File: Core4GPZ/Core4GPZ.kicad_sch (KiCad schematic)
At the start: 3 parts, among them U1 core4, U2 MPX4250

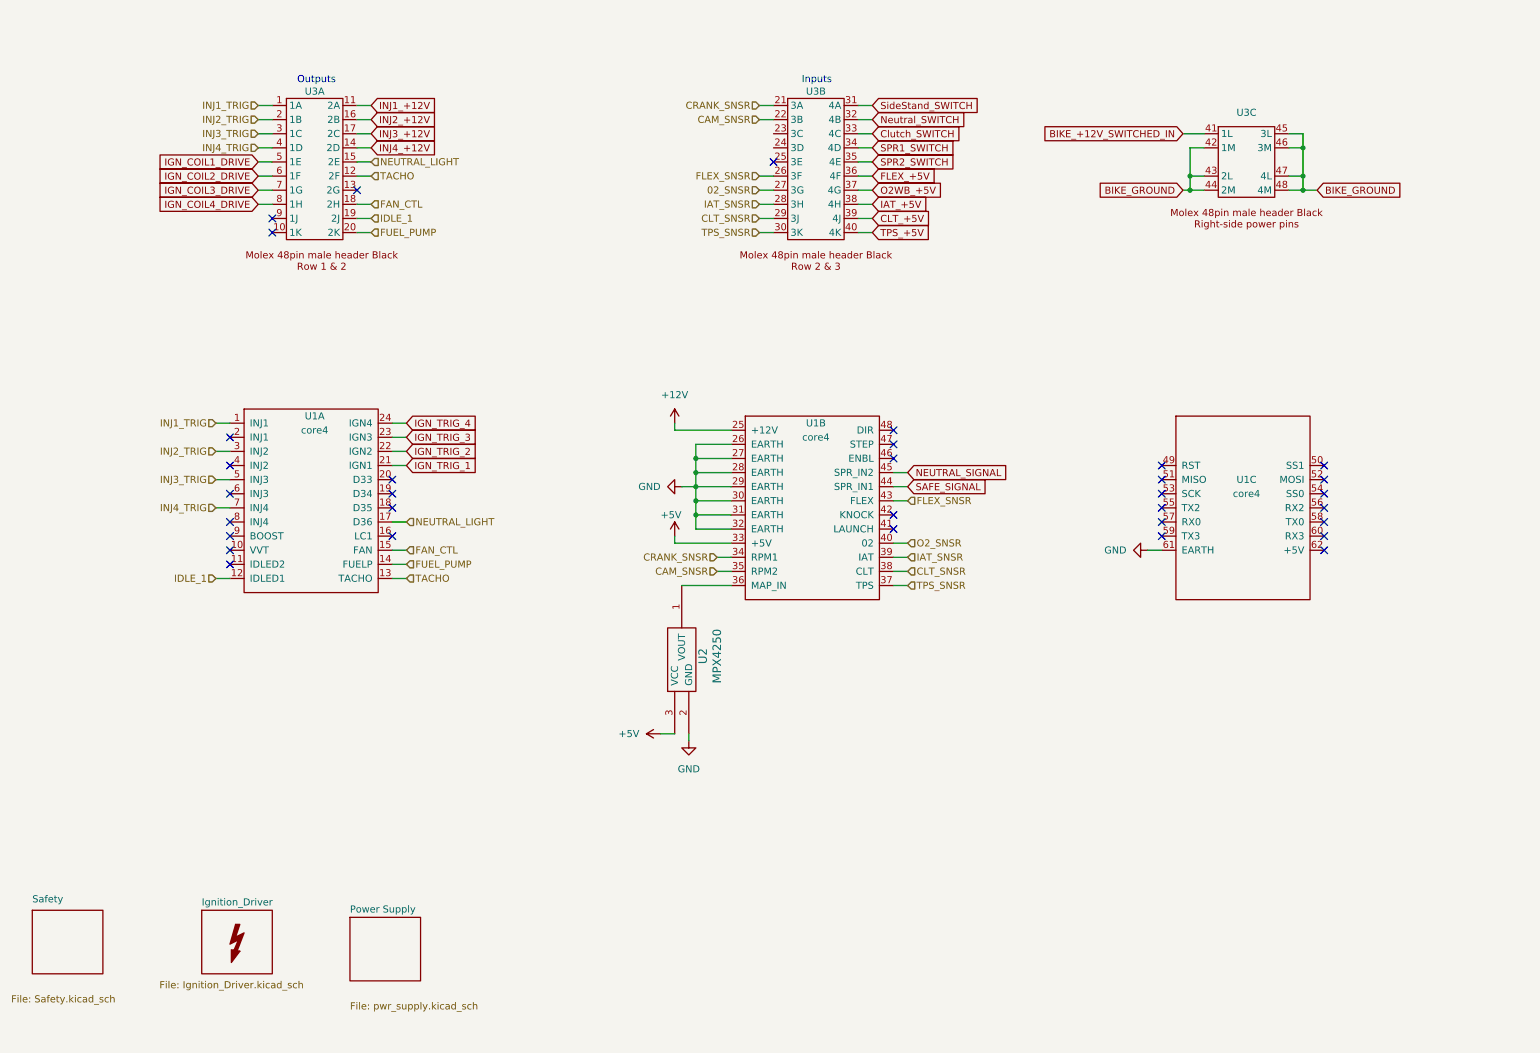
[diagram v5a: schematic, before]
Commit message: Added VR Conditionner for Cam/Crank SNSR
Added some jumper for prototyping and testing purposes
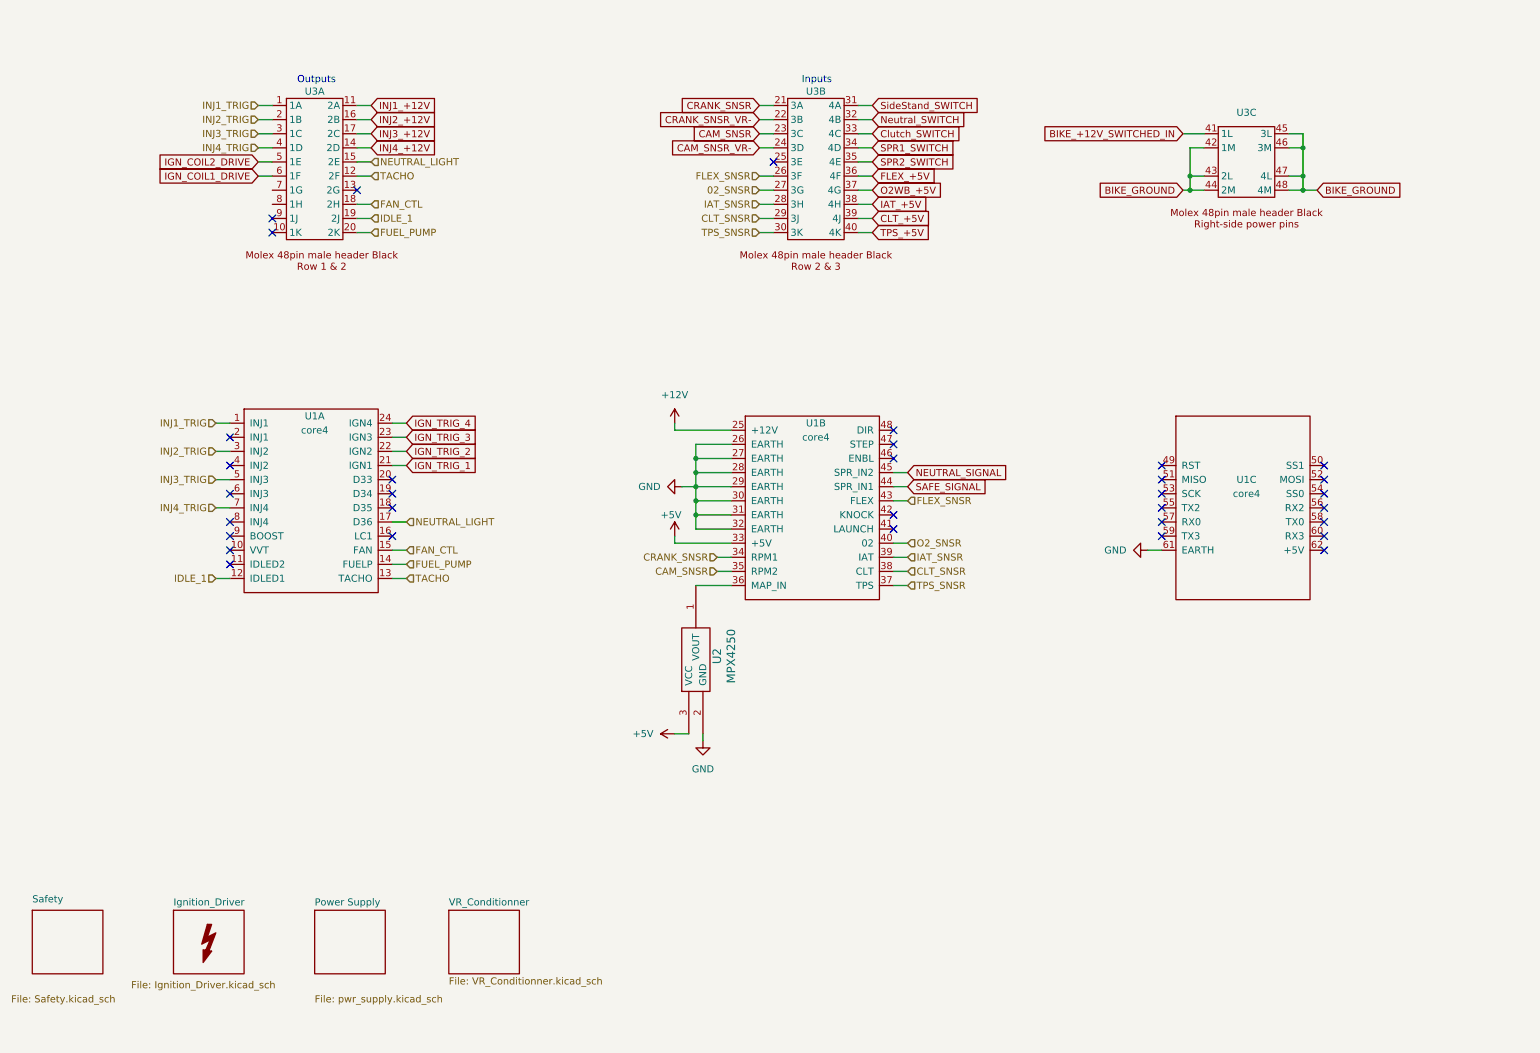
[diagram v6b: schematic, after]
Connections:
- net CAM_SNSR: now also U3.23 (3C); no longer U3.22 (3B)
- net IGN_COIL1_DRIVE: now also U3.6 (1F); no longer U3.5 (1E)
- net IGN_COIL2_DRIVE: now also U3.5 (1E); no longer U3.6 (1F)
- net CAM_SNSR_VR-: now reaches U3.24 (3D)
- net IGN_COIL3_DRIVE: no longer names the net of U3.7 (1G)
- net IGN_COIL4_DRIVE: no longer names the net of U3.8 (1H)
- new net CRANK_SNSR_VR-: U3.22 (3B)
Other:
- added sheet VR_Conditionner (VR_Conditionner.kicad_sch)
- moved on the sheet: U2

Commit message: Started Implementation of VR Conditionner
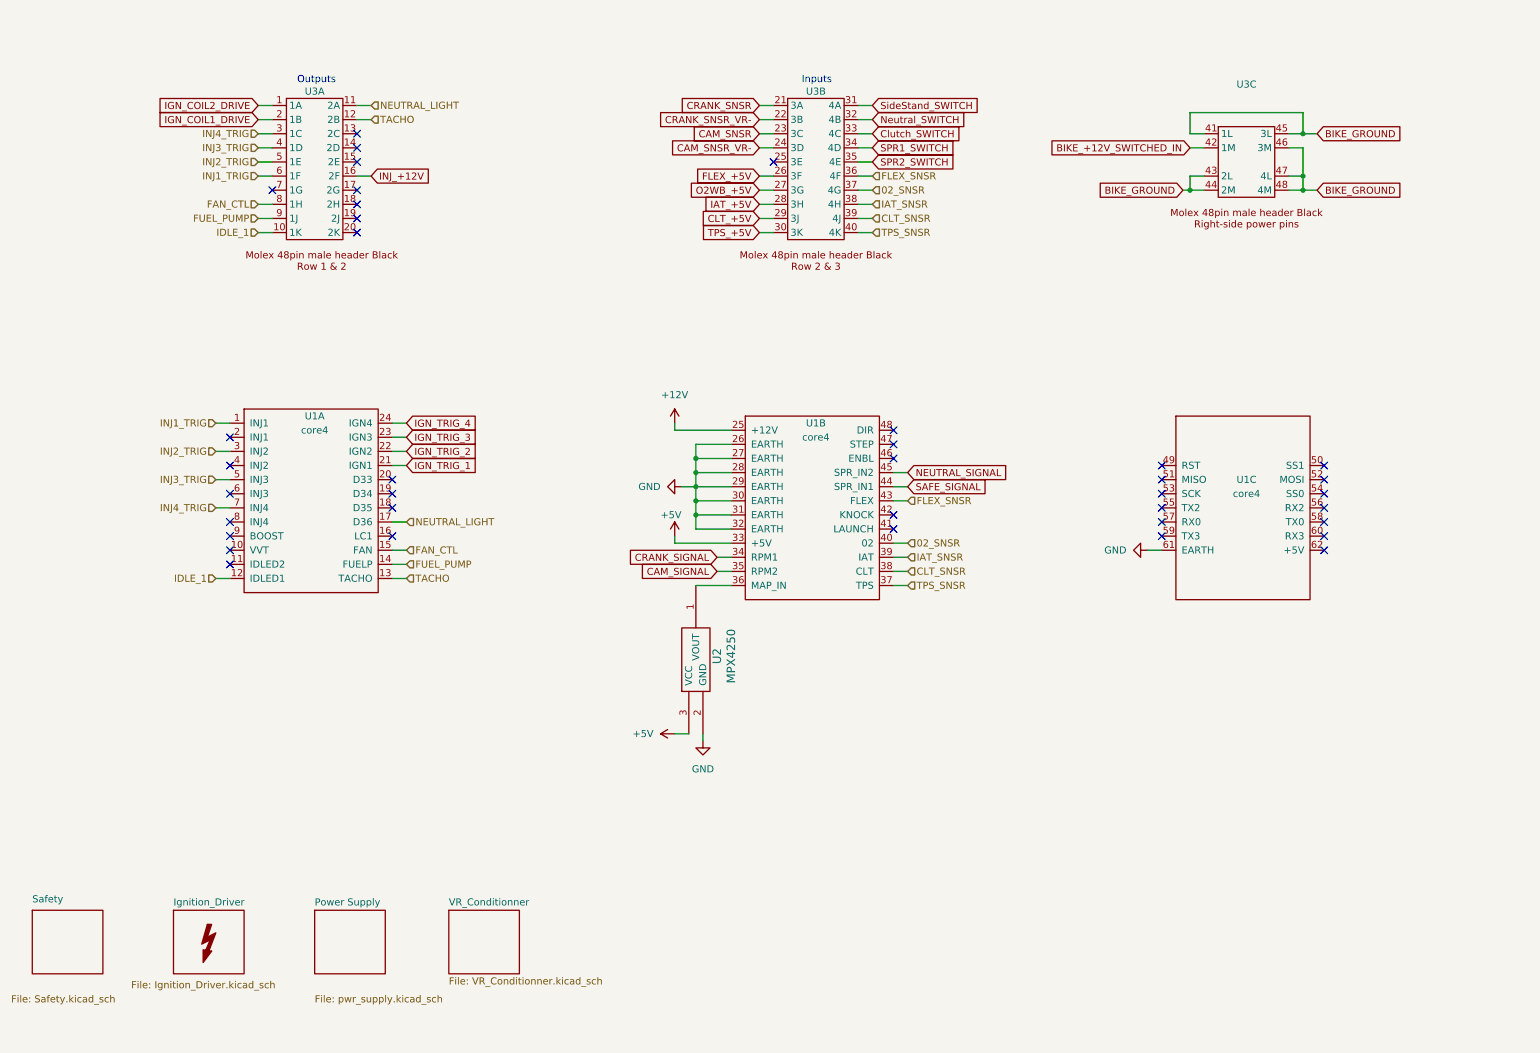
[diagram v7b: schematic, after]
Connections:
- net INJ1_+12V is gone; now on net NEUTRAL_LIGHT: U3.11 (2A)
- net O2_SNSR is gone; now on net 02_SNSR: U1.40 (02)
- net 02_SNSR: now also U3.37 (4G); no longer U3.27 (3G)
- net BIKE_+12V_SWITCHED_IN: now also U3.42 (1M); no longer U3.41 (1L)
- net BIKE_GROUND: now also U3.41 (1L); no longer U3.42 (1M)
- net CAM_SNSR: no longer U1.35 (RPM2)
- net CLT_+5V: now also U3.29 (3J); no longer U3.39 (4J)
- net CLT_SNSR: now also U3.39 (4J); no longer U3.29 (3J)
- net CRANK_SNSR: no longer U1.34 (RPM1)
- net FAN_CTL: now also U3.8 (1H); no longer U3.18 (2H)
- net FLEX_+5V: now also U3.26 (3F); no longer U3.36 (4F)
- net FLEX_SNSR: now also U3.36 (4F); no longer U3.26 (3F)
- net FUEL_PUMP: now also U3.9 (1J); no longer U3.20 (2K)
- net IAT_+5V: now also U3.28 (3H); no longer U3.38 (4H)
- net IAT_SNSR: now also U3.38 (4H); no longer U3.28 (3H)
- net IDLE_1: now also U3.10 (1K); no longer U3.19 (2J)
- net IGN_COIL1_DRIVE: now also U3.2 (1B); no longer U3.6 (1F)
- net IGN_COIL2_DRIVE: now also U3.1 (1A); no longer U3.5 (1E)
- net INJ1_TRIG: now also U3.6 (1F); no longer U3.1 (1A)
- net INJ2_TRIG: now also U3.5 (1E); no longer U3.2 (1B)
- net INJ3_TRIG: now also U3.4 (1D); no longer U3.3 (1C)
- net INJ4_TRIG: now also U3.3 (1C); no longer U3.4 (1D)
- net NEUTRAL_LIGHT: no longer U3.15 (2E)
- net O2WB_+5V: now also U3.27 (3G); no longer U3.37 (4G)
- net TPS_+5V: now also U3.30 (3K); no longer U3.40 (4K)
- net TPS_SNSR: now also U3.40 (4K); no longer U3.30 (3K)
- net INJ2_+12V renamed INJ_+12V
- net INJ3_+12V: no longer names the net of U3.17 (2G)
- net INJ4_+12V: no longer names the net of U3.14 (2D)
- new net CAM_SIGNAL: U1.35 (RPM2)
- new net CRANK_SIGNAL: U1.34 (RPM1)
- no-connect marks 33 -> 38

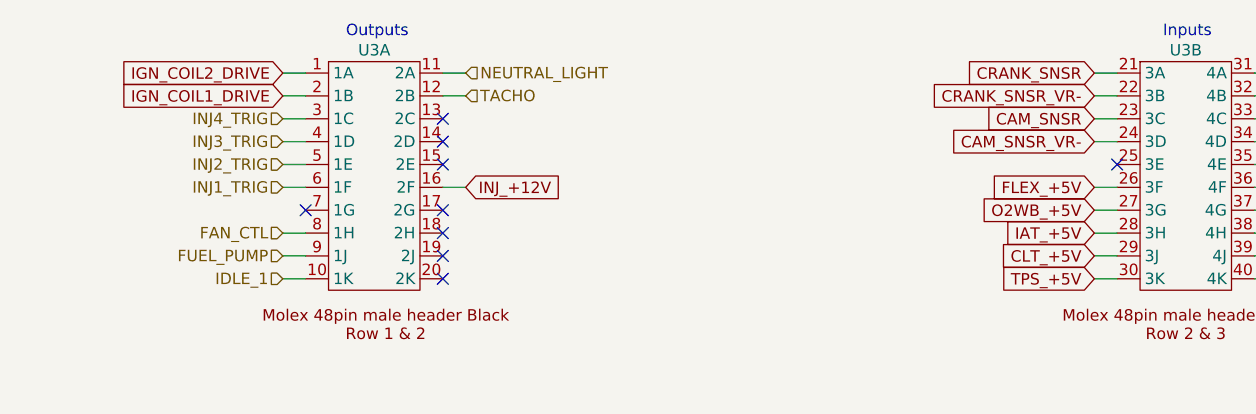
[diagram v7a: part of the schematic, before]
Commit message: Implemented VR_Conditionner (MAX9926+)
First look at ground plane
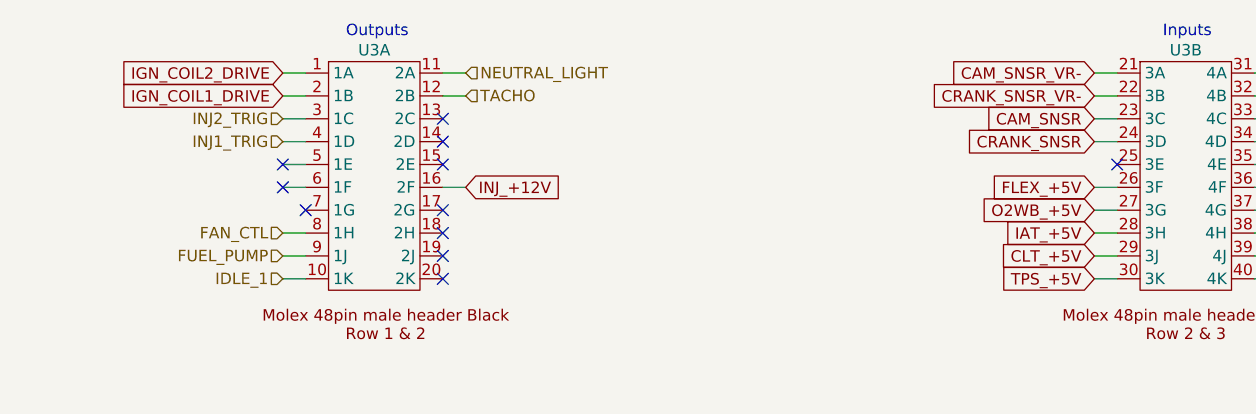
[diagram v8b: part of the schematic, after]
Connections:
- net CAM_SNSR_VR-: now also U3.21 (3A); no longer U3.24 (3D)
- net CRANK_SNSR: now also U3.24 (3D); no longer U3.21 (3A)
- net INJ1_TRIG: now also U3.4 (1D); no longer U3.6 (1F)
- net INJ2_TRIG: now also U3.3 (1C); no longer U3.5 (1E)
- net INJ3_TRIG: no longer U3.4 (1D)
- net INJ4_TRIG: no longer U3.3 (1C)
- no-connect marks 38 -> 40
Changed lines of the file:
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@@
+	)
+	(no_connect
+		(at 58.42 41.91)
 	)
 	(no_connect
@@
 	(no_connect
 		(at 76.2 39.37)
+	)
+	(no_connect
+		(at 58.42 39.37)
 	)
 	(no_connect
@@
 	(global_label "CAM_SNSR_VR-"
 		(shape input)
+		(at 148.59 29.21 180)
+		(fields_autoplaced yes)
+		(effects
+			(font
+				(size 1.27 1.27)
+			)
+			(justify right)
+		)
+		(property "Intersheetrefs" "${INTERSHEET_REFS}"
+			(at 130.9091 29.21 0)
+			(effects
+				(font
+					(size 1.27 1.27)
+				)
+				(justify right)
+				(hide yes)
+			)
+		)
+	)
+	(global_label "CRANK_SNSR"
+		(shape input)
 		(at 148.59 36.83 180)
 		(fields_autoplaced yes)
@@
 		)
 		(property "Intersheetrefs" "${INTERSHEET_REFS}"
-			(at 130.9091 36.83 0)
+			(at 133.3886 36.83 0)
 			(effects
 				(font
@@
 		)
 	)
-	(global_label "CRANK_SNSR"
-		(shape input)
-		(at 148.59 29.21 180)
-		(fields_autoplaced yes)
-		(effects
-			(font
-				(size 1.27 1.27)
-			)
-			(justify right)
-		)
-		(property "Intersheetrefs" "${INTERSHEET_REFS}"
-			(at 133.3886 29.21 0)
+	(global_label "SPR1_SWITCH"
+		(shape input)
+		(at 168.91 36.83 0)
+		(fields_autoplaced yes)
+		(effects
+			(font
+				(size 1.27 1.27)
+			)
+			(justify left)
+		)
+		(property "Intersheetrefs" "${INTERSHEET_REFS}"
+			(at 184.6556 36.83 0)
+			(effects
+				(font
+					(size 1.27 1.27)
+				)
+				(justify left)
+				(hide yes)
+			)
+		)
+	)
+	(global_label "IGN_TRIG_4"
+		(shape input)
+		(at 85.09 86.36 0)
+		(fields_autoplaced yes)
+		(effects
+			(font
+				(size 1.27 1.27)
+			)
+			(justify left)
+		)
+		(property "Intersheetrefs" "${INTERSHEET_REFS}"
+			(at 98.5376 86.36 0)
+			(effects
+				(font
+					(size 1.27 1.27)
+				)
+				(justify left)
+				(hide yes)
+			)
+		)
+	)
+	(global_label "IAT_+5V"
+		(shape input)
+		(at 148.59 46.99 180)
+		(fields_autoplaced yes)
+		(effects
+			(font
+				(size 1.27 1.27)
+			)
+			(justify right)
+		)
+		(property "Intersheetrefs" "${INTERSHEET_REFS}"
+			(at 138.1057 46.99 0)
 			(effects
 				(font
@@
 		)
 	)
-	(global_label "SPR1_SWITCH"
-		(shape input)
-		(at 168.91 36.83 0)
-		(fields_autoplaced yes)
-		(effects
-			(font
-				(size 1.27 1.27)
-			)
-			(justify left)
-		)
-		(property "Intersheetrefs" "${INTERSHEET_REFS}"
-			(at 184.6556 36.83 0)
+	(global_label "Clutch_SWITCH"
+		(shape input)
+		(at 168.91 34.29 0)
+		(fields_autoplaced yes)
+		(effects
+			(font
+				(size 1.27 1.27)
+			)
+			(justify left)
+		)
+		(property "Intersheetrefs" "${INTERSHEET_REFS}"
+			(at 185.7441 34.29 0)
 			(effects
 				(font
@@
 		)
 	)
-	(global_label "IGN_TRIG_4"
-		(shape input)
-		(at 85.09 86.36 0)
-		(fields_autoplaced yes)
-		(effects
-			(font
-				(size 1.27 1.27)
-			)
-			(justify left)
-		)
-		(property "Intersheetrefs" "${INTERSHEET_REFS}"
-			(at 98.5376 86.36 0)
-			(effects
-				(font
-					(size 1.27 1.27)
-				)
-				(justify left)
-				(hide yes)
-			)
-		)
-	)
-	(global_label "IAT_+5V"
-		(shape input)
-		(at 148.59 46.99 180)
-		(fields_autoplaced yes)
-		(effects
-			(font
-				(size 1.27 1.27)
-			)
-			(justify right)
-		)
-		(property "Intersheetrefs" "${INTERSHEET_REFS}"
-			(at 138.1057 46.99 0)
+	(global_label "IGN_COIL1_DRIVE"
+		(shape input)
+		(at 58.42 31.75 180)
+		(fields_autoplaced yes)
+		(effects
+			(font
+				(size 1.27 1.27)
+			)
+			(justify right)
+		)
+		(property "Intersheetrefs" "${INTERSHEET_REFS}"
+			(at 39.469 31.75 0)
 			(effects
 				(font
@@
 		)
 	)
-	(global_label "Clutch_SWITCH"
-		(shape input)
-		(at 168.91 34.29 0)
-		(fields_autoplaced yes)
-		(effects
-			(font
-				(size 1.27 1.27)
-			)
-			(justify left)
-		)
-		(property "Intersheetrefs" "${INTERSHEET_REFS}"
-			(at 185.7441 34.29 0)
-			(effects
-				(font
-					(size 1.27 1.27)
-				)
-				(justify left)
-				(hide yes)
-			)
-		)
-	)
-	(global_label "IGN_COIL1_DRIVE"
-		(shape input)
-		(at 58.42 31.75 180)
-		(fields_autoplaced yes)
-		(effects
-			(font
-				(size 1.27 1.27)
-			)
-			(justify right)
-		)
-		(property "Intersheetrefs" "${INTERSHEET_REFS}"
-			(at 39.469 31.75 0)
+	(global_label "CLT_+5V"
+		(shape input)
+		(at 148.59 49.53 180)
+		(fields_autoplaced yes)
+		(effects
+			(font
+				(size 1.27 1.27)
+			)
+			(justify right)
+		)
+		(property "Intersheetrefs" "${INTERSHEET_REFS}"
+			(at 137.501 49.53 0)
 			(effects
 				(font
@@
 		)
 	)
-	(global_label "CLT_+5V"
-		(shape input)
-		(at 148.59 49.53 180)
-		(fields_autoplaced yes)
-		(effects
-			(font
-				(size 1.27 1.27)
-			)
-			(justify right)
-		)
-		(property "Intersheetrefs" "${INTERSHEET_REFS}"
-			(at 137.501 49.53 0)
-			(effects
-				(font
-					(size 1.27 1.27)
-				)
-				(justify right)
-				(hide yes)
-			)
-		)
-	)
 	(hierarchical_label "FUEL_PUMP"
 		(shape input)
@@
 		)
 	)
+	(hierarchical_label "INJ2_TRIG"
+		(shape input)
+		(at 58.42 34.29 180)
+		(fields_autoplaced yes)
+		(effects
+			(font
+				(size 1.27 1.27)
+			)
+			(justify right)
+		)
+	)
+	(hierarchical_label "INJ1_TRIG"
+		(shape input)
+		(at 50.8 86.36 180)
+		(fields_autoplaced yes)
+		(effects
+			(font
+				(size 1.27 1.27)
+			)
+			(justify right)
+		)
+	)
+	(hierarchical_label "INJ3_TRIG"
+		(shape input)
+		(at 50.8 96.52 180)
+		(fields_autoplaced yes)
+		(effects
+			(font
+				(size 1.27 1.27)
+			)
+			(justify right)
+		)
+	)
+	(hierarchical_label "TACHO"
+		(shape input)
+		(at 78.74 31.75 0)
+		(fields_autoplaced yes)
+		(effects
+			(font
+				(size 1.27 1.27)
+			)
+			(justify left)
+		)
+	)
 	(hierarchical_label "INJ4_TRIG"
 		(shape input)
-		(at 58.42 34.29 180)
-		(fields_autoplaced yes)
-		(effects
-			(font
-				(size 1.27 1.27)
-			)
-			(justify right)
-		)
-	)
-	(hierarchical_label "INJ2_TRIG"
-		(shape input)
-		(at 58.42 39.37 180)
-		(fields_autoplaced yes)
-		(effects
-			(font
-				(size 1.27 1.27)
-			)
-			(justify right)
+		(at 50.8 101.6 180)
+		(fields_autoplaced yes)
+		(effects
+			(font
+				(size 1.27 1.27)
+			)
+			(justify right)
+		)
+	)
+	(hierarchical_label "CLT_SNSR"
+		(shape input)
+		(at 175.26 113.03 0)
+		(fields_autoplaced yes)
+		(effects
+			(font
+				(size 1.27 1.27)
+			)
+			(justify left)
+		)
+	)
+	(hierarchical_label "NEUTRAL_LIGHT"
+		(shape input)
+		(at 85.09 104.14 0)
+		(fields_autoplaced yes)
+		(effects
+			(font
+				(size 1.27 1.27)
+			)
+			(justify left)
 		)
 	)
 	(hierarchical_label "INJ1_TRIG"
 		(shape input)
-		(at 50.8 86.36 180)
-		(fields_autoplaced yes)
-		(effects
-			(font
-				(size 1.27 1.27)
-			)
-			(justify right)
-		)
-	)
-	(hierarchical_label "INJ3_TRIG"
-		(shape input)
-		(at 50.8 96.52 180)
-		(fields_autoplaced yes)
-		(effects
-			(font
-				(size 1.27 1.27)
-			)
-			(justify right)
-		)
-	)
-	(hierarchical_label "TACHO"
-		(shape input)
-		(at 78.74 31.75 0)
-		(fields_autoplaced yes)
-		(effects
-			(font
-				(size 1.27 1.27)
-			)
-			(justify left)
-		)
-	)
-	(hierarchical_label "INJ4_TRIG"
-		(shape input)
-		(at 50.8 101.6 180)
-		(fields_autoplaced yes)
-		(effects
-			(font
-				(size 1.27 1.27)
-			)
-			(justify right)
-		)
-	)
-	(hierarchical_label "CLT_SNSR"
-		(shape input)
-		(at 175.26 113.03 0)
-		(fields_autoplaced yes)
-		(effects
-			(font
-				(size 1.27 1.27)
-			)
-			(justify left)
-		)
-	)
-	(hierarchical_label "NEUTRAL_LIGHT"
-		(shape input)
-		(at 85.09 104.14 0)
-		(fields_autoplaced yes)
-		(effects
-			(font
-				(size 1.27 1.27)
-			)
-			(justify left)
-		)
-	)
-	(hierarchical_label "INJ1_TRIG"
-		(shape input)
-		(at 58.42 41.91 180)
+		(at 58.42 36.83 180)
 		(fields_autoplaced yes)
 		(effects
@@
 		)
 	)
-	(hierarchical_label "INJ3_TRIG"
-		(shape input)
-		(at 58.42 36.83 180)
-		(fields_autoplaced yes)
-		(effects
-			(font
-				(size 1.27 1.27)
-			)
-			(justify right)
-		)
-	)
